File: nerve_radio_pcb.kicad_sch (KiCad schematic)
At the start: 26 parts, among them J1 BF030-20A-B1-0360-0277-0600-LB, J15 5V GPIO Breakout, J16 3V SPI Breakout, J2 Battery, U1 LMR51430, U2 TXB0104QPWRQ1, U3 XBP9B-DMWT-002

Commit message: Move UART RX/TX flip to board-to-board connector
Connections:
- net RADIO_UART_RX: now also J1.7, U3.3 (DIN/~{CONFIG}/DIO14); no longer J1.5, U3.2 (DOUT/DIO13)
- net RADIO_UART_TX: now also J1.5, U3.2 (DOUT/DIO13); no longer J1.7, U3.3 (DIN/~{CONFIG}/DIO14)
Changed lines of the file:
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@@
+		)
+	)
+	(hierarchical_label "RADIO_UART_TX"
+		(shape input)
+		(at 82.55 99.06 0)
+		(effects
+			(font
+				(size 1.27 1.27)
+			)
+			(justify left)
+		)
+	)
+	(hierarchical_label "RADIO_UART_RX"
+		(shape input)
+		(at 57.15 34.29 0)
+		(effects
+			(font
+				(size 1.27 1.27)
+			)
+			(justify left)
 		)
 	)
@@
 		)
 	)
+	(hierarchical_label "RADIO_UART_TX"
+		(shape input)
+		(at 57.15 31.75 0)
+		(effects
+			(font
+				(size 1.27 1.27)
+			)
+			(justify left)
+		)
+	)
+	(hierarchical_label "SPI_CLK"
+		(shape input)
+		(at 44.45 44.45 180)
+		(effects
+			(font
+				(size 1.27 1.27)
+			)
+			(justify right)
+		)
+	)
+	(hierarchical_label "SPI_CS"
+		(shape input)
+		(at 44.45 46.99 180)
+		(effects
+			(font
+				(size 1.27 1.27)
+			)
+			(justify right)
+		)
+	)
+	(hierarchical_label "GPIO_2{slash}PWM_2_{5V}"
+		(shape input)
+		(at 264.16 39.37 0)
+		(effects
+			(font
+				(size 1.27 1.27)
+			)
+			(justify left)
+		)
+	)
+	(hierarchical_label "GPIO_1{slash}PWM_1_{5V}"
+		(shape input)
+		(at 215.9 151.13 180)
+		(effects
+			(font
+				(size 1.27 1.27)
+			)
+			(justify right)
+		)
+	)
 	(hierarchical_label "RADIO_UART_RX"
 		(shape input)
-		(at 57.15 31.75 0)
-		(effects
-			(font
-				(size 1.27 1.27)
-			)
-			(justify left)
-		)
-	)
-	(hierarchical_label "RADIO_UART_RX"
-		(shape input)
-		(at 82.55 99.06 0)
-		(effects
-			(font
-				(size 1.27 1.27)
-			)
-			(justify left)
+		(at 31.75 99.06 180)
+		(effects
+			(font
+				(size 1.27 1.27)
+			)
+			(justify right)
+		)
+	)
+	(hierarchical_label "SPI_MISO"
+		(shape input)
+		(at 57.15 41.91 0)
+		(effects
+			(font
+				(size 1.27 1.27)
+			)
+			(justify left)
+		)
+	)
+	(hierarchical_label "SPI_CS"
+		(shape input)
+		(at 254 156.21 180)
+		(effects
+			(font
+				(size 1.27 1.27)
+			)
+			(justify right)
+		)
+	)
+	(hierarchical_label "GPIO_2{slash}PWM_2_{5V}"
+		(shape input)
+		(at 215.9 153.67 180)
+		(effects
+			(font
+				(size 1.27 1.27)
+			)
+			(justify right)
+		)
+	)
+	(hierarchical_label "GPIO_2{slash}PWM_2{slash}ADC_DRDY"
+		(shape input)
+		(at 243.84 39.37 180)
+		(effects
+			(font
+				(size 1.27 1.27)
+			)
+			(justify right)
+		)
+	)
+	(hierarchical_label "SPI_MOSI"
+		(shape input)
+		(at 254 151.13 180)
+		(effects
+			(font
+				(size 1.27 1.27)
+			)
+			(justify right)
+		)
+	)
+	(hierarchical_label "SPI_MOSI"
+		(shape input)
+		(at 57.15 44.45 0)
+		(effects
+			(font
+				(size 1.27 1.27)
+			)
+			(justify left)
+		)
+	)
+	(hierarchical_label "SPI_MISO"
+		(shape input)
+		(at 254 148.59 180)
+		(effects
+			(font
+				(size 1.27 1.27)
+			)
+			(justify right)
+		)
+	)
+	(hierarchical_label "RADIO_UART_RTS"
+		(shape input)
+		(at 44.45 34.29 180)
+		(effects
+			(font
+				(size 1.27 1.27)
+			)
+			(justify right)
+		)
+	)
+	(hierarchical_label "RADIO_NRST"
+		(shape input)
+		(at 44.45 36.83 180)
+		(effects
+			(font
+				(size 1.27 1.27)
+			)
+			(justify right)
 		)
 	)
 	(hierarchical_label "SPI_CLK"
 		(shape input)
-		(at 44.45 44.45 180)
-		(effects
-			(font
-				(size 1.27 1.27)
-			)
-			(justify right)
-		)
-	)
-	(hierarchical_label "SPI_CS"
-		(shape input)
-		(at 44.45 46.99 180)
-		(effects
-			(font
-				(size 1.27 1.27)
-			)
-			(justify right)
-		)
-	)
-	(hierarchical_label "GPIO_2{slash}PWM_2_{5V}"
-		(shape input)
-		(at 264.16 39.37 0)
-		(effects
-			(font
-				(size 1.27 1.27)
-			)
-			(justify left)
+		(at 254 153.67 180)
+		(effects
+			(font
+				(size 1.27 1.27)
+			)
+			(justify right)
+		)
+	)
+	(hierarchical_label "RADIO_UART_CTS"
+		(shape input)
+		(at 44.45 31.75 180)
+		(effects
+			(font
+				(size 1.27 1.27)
+			)
+			(justify right)
 		)
 	)
 	(hierarchical_label "GPIO_1{slash}PWM_1_{5V}"
 		(shape input)
-		(at 215.9 151.13 180)
-		(effects
-			(font
-				(size 1.27 1.27)
-			)
-			(justify right)
-		)
-	)
-	(hierarchical_label "SPI_MISO"
-		(shape input)
-		(at 57.15 41.91 0)
-		(effects
-			(font
-				(size 1.27 1.27)
-			)
-			(justify left)
-		)
-	)
-	(hierarchical_label "SPI_CS"
-		(shape input)
-		(at 254 156.21 180)
-		(effects
-			(font
-				(size 1.27 1.27)
-			)
-			(justify right)
-		)
-	)
-	(hierarchical_label "GPIO_2{slash}PWM_2_{5V}"
-		(shape input)
-		(at 215.9 153.67 180)
-		(effects
-			(font
-				(size 1.27 1.27)
-			)
-			(justify right)
+		(at 264.16 36.83 0)
+		(effects
+			(font
+				(size 1.27 1.27)
+			)
+			(justify left)
+		)
+	)
+	(hierarchical_label "RADIO_UART_CTS"
+		(shape input)
+		(at 82.55 101.6 0)
+		(effects
+			(font
+				(size 1.27 1.27)
+			)
+			(justify left)
 		)
 	)
 	(hierarchical_label "GPIO_2{slash}PWM_2{slash}ADC_DRDY"
 		(shape input)
-		(at 243.84 39.37 180)
-		(effects
-			(font
-				(size 1.27 1.27)
-			)
-			(justify right)
-		)
-	)
-	(hierarchical_label "SPI_MOSI"
-		(shape input)
-		(at 254 151.13 180)
-		(effects
-			(font
-				(size 1.27 1.27)
-			)
-			(justify right)
-		)
-	)
-	(hierarchical_label "SPI_MOSI"
-		(shape input)
-		(at 57.15 44.45 0)
-		(effects
-			(font
-				(size 1.27 1.27)
-			)
-			(justify left)
-		)
-	)
-	(hierarchical_label "SPI_MISO"
-		(shape input)
-		(at 254 148.59 180)
-		(effects
-			(font
-				(size 1.27 1.27)
-			)
-			(justify right)
-		)
-	)
-	(hierarchical_label "RADIO_UART_RTS"
-		(shape input)
-		(at 44.45 34.29 180)
-		(effects
-			(font
-				(size 1.27 1.27)
-			)
-			(justify right)
-		)
-	)
-	(hierarchical_label "RADIO_NRST"
-		(shape input)
-		(at 44.45 36.83 180)
-		(effects
-			(font
-				(size 1.27 1.27)
-			)
-			(justify right)
-		)
-	)
-	(hierarchical_label "SPI_CLK"
-		(shape input)
-		(at 254 153.67 180)
-		(effects
-			(font
-				(size 1.27 1.27)
-			)
-			(justify right)
-		)
-	)
-	(hierarchical_label "RADIO_UART_CTS"
-		(shape input)
-		(at 44.45 31.75 180)
-		(effects
-			(font
-				(size 1.27 1.27)
-			)
-			(justify right)
-		)
-	)
-	(hierarchical_label "GPIO_1{slash}PWM_1_{5V}"
-		(shape input)
-		(at 264.16 36.83 0)
-		(effects
-			(font
-				(size 1.27 1.27)
-			)
-			(justify left)
-		)
-	)
-	(hierarchical_label "RADIO_UART_CTS"
-		(shape input)
-		(at 82.55 101.6 0)
-		(effects
-			(font
-				(size 1.27 1.27)
-			)
-			(justify left)
-		)
-	)
-	(hierarchical_label "GPIO_2{slash}PWM_2{slash}ADC_DRDY"
-		(shape input)
 		(at 44.45 41.91 180)
 		(effects
@@
 		)
 	)
-	(hierarchical_label "RADIO_UART_TX"
-		(shape input)
-		(at 31.75 99.06 180)
-		(effects
-			(font
-				(size 1.27 1.27)
-			)
-			(justify right)
-		)
-	)
-	(hierarchical_label "RADIO_UART_TX"
-		(shape input)
-		(at 57.15 34.29 0)
-		(effects
-			(font
-				(size 1.27 1.27)
-			)
-			(justify left)
-		)
-	)

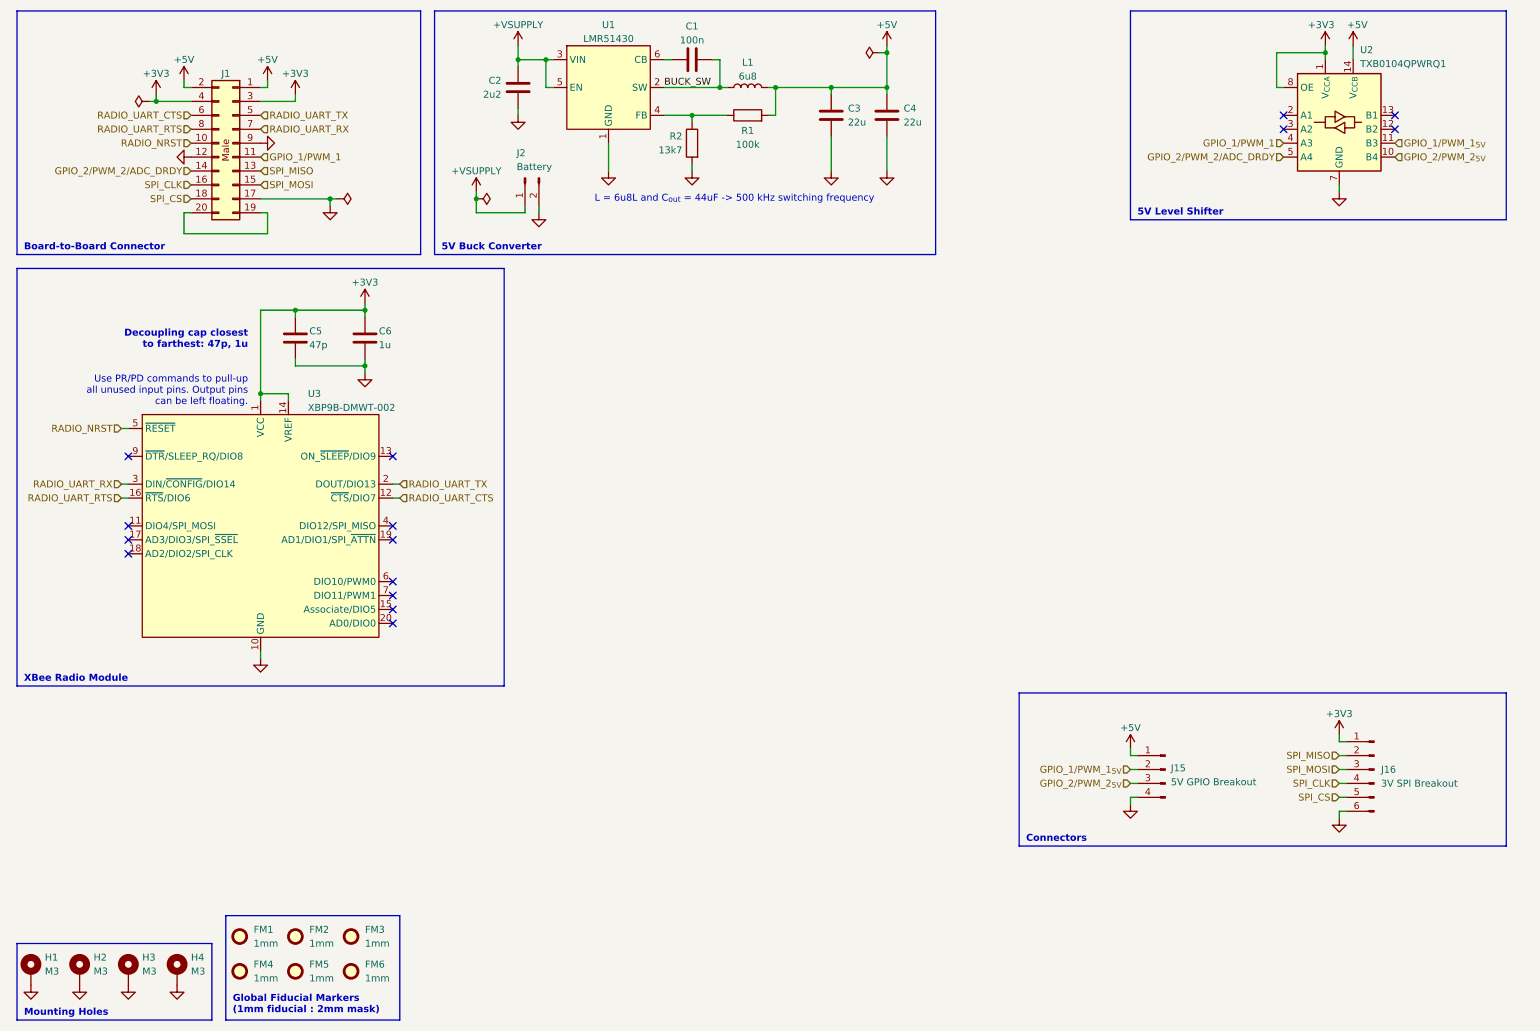
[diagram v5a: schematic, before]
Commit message: Add minor decoupling caps and TVS/Schottky diodes
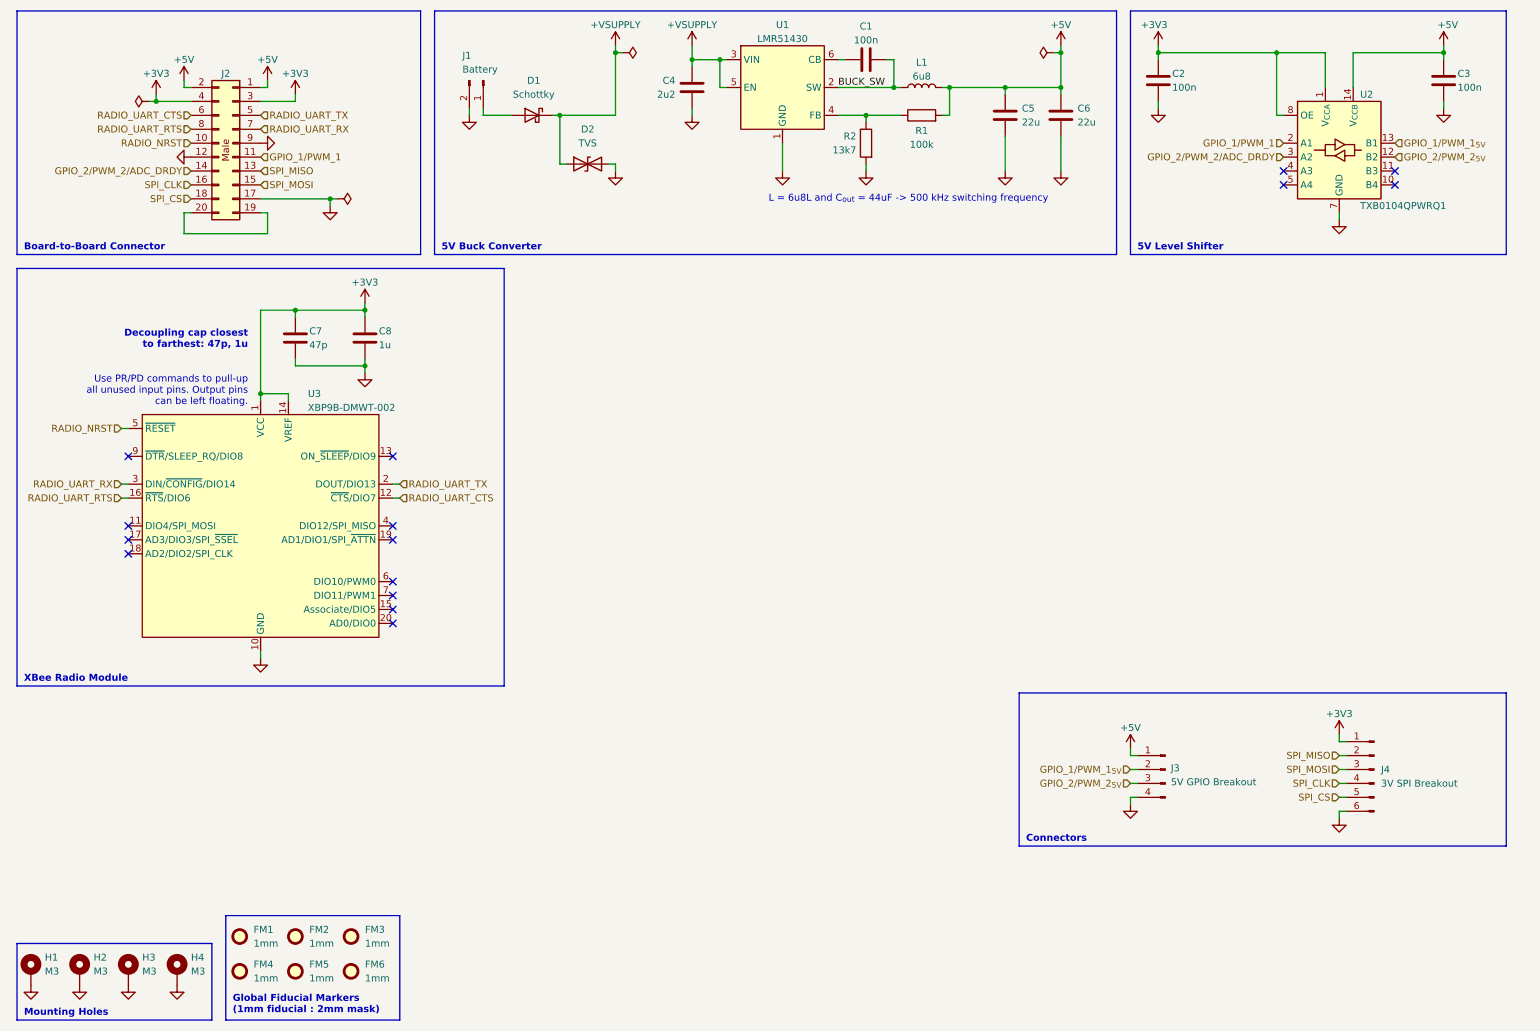
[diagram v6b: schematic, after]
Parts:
- added C2, C3: 100n, Capacitor_SMD:C_0603_1608Metric, symbol Device:C
- added D1: Schottky, Diode_SMD:D_SMA, symbol Device:D_Schottky
- added D2: TVS, Diode_SMD:D_SMA, symbol Device:D_TVS
- renumbered C2 to C4, C3 to C5, C4 to C6, C5 to C7, C6 to C8, J2 to J1, J1 to J2, J15 to J3, J16 to J4
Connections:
- net +3V3: now also C2.1
- net +5V: now also C3.1
- net +VSUPPLY: now also D1.1 (K), D2.1 (A1); no longer J1.1 (Pin_1)
- net GND: now also C2.2, C3.2, D2.2 (A2)
- net GPIO_1/PWM_1: now also U2.2 (A1); no longer U2.4 (A3)
- net GPIO_1/PWM_1_{5V}: now also U2.13 (B1); no longer U2.11 (B3)
- net GPIO_2/PWM_2_{5V}: now also U2.12 (B2); no longer U2.10 (B4)
- net GPIO_2/PWM_2/ADC_DRDY: now also U2.3 (A2); no longer U2.5 (A4)
- new net: D1.2 (A), J1.1 (Pin_1)
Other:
- moved on the sheet: C1, C4, C5, C6, J1, L1, R1, R2, U1, U2

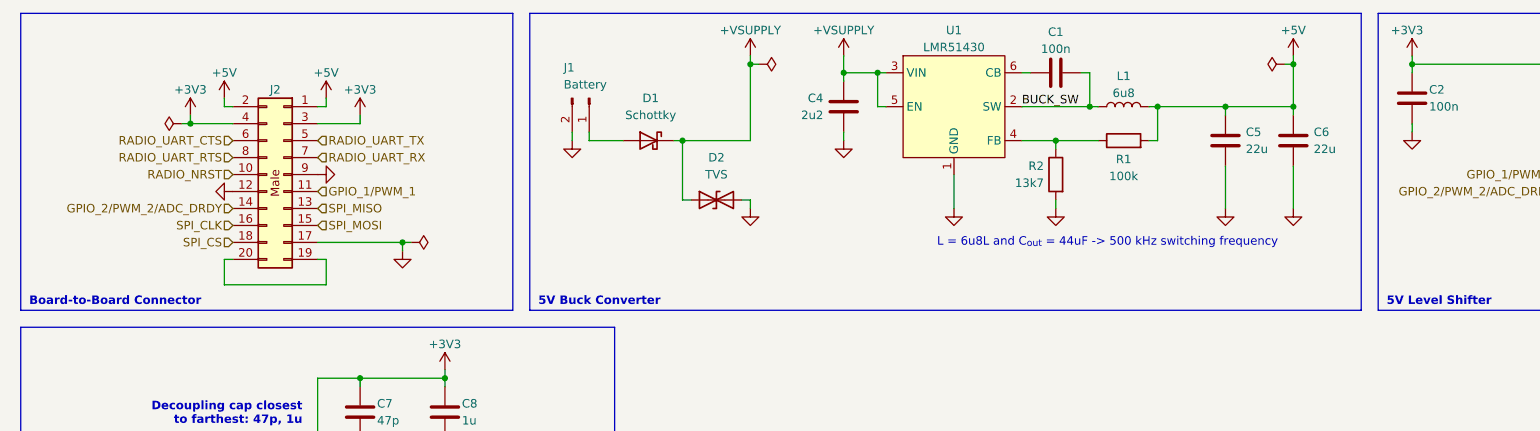
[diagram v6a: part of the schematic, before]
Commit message: Add TVS and schottky diode info
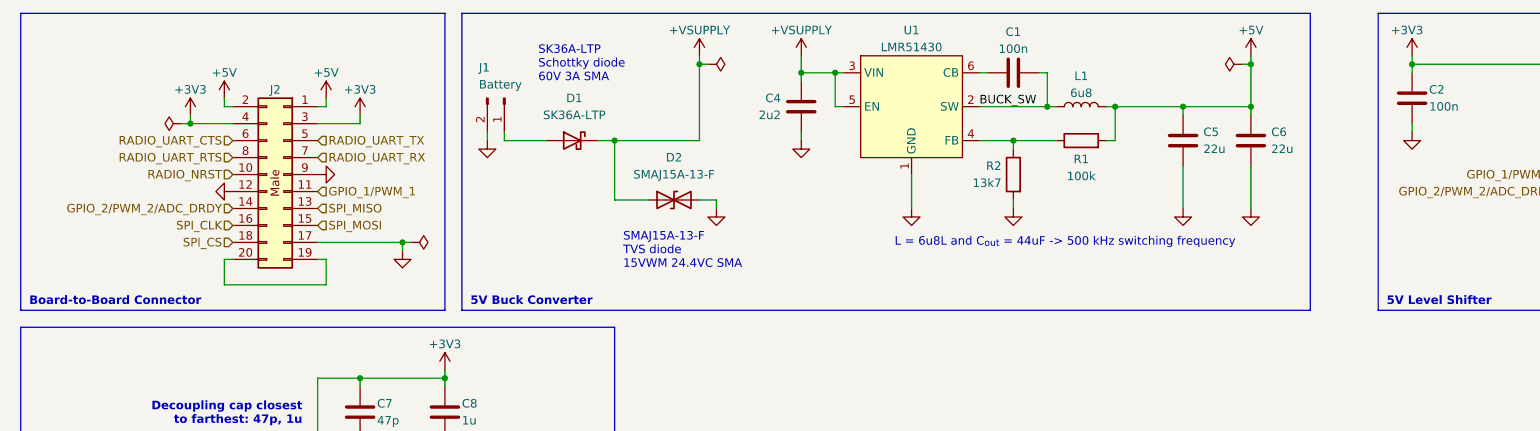
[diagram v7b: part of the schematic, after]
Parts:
- D1: value Schottky -> SK36A-LTP
- D2: value TVS -> SMAJ15A-13-F
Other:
- note added: "SK36A-LTP Schottky diode 60V 3A SMA"
- note added: "SMAJ15A-13-F TVS diode 15VWM 24.4VC SMA"
- moved on the sheet: C1, C4, C5, C6, D1, D2, J1, L1, R1, R2, U1
